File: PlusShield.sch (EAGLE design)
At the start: 32 parts, among them K1 G6J-2P-Y, K2 G6J-2P-Y

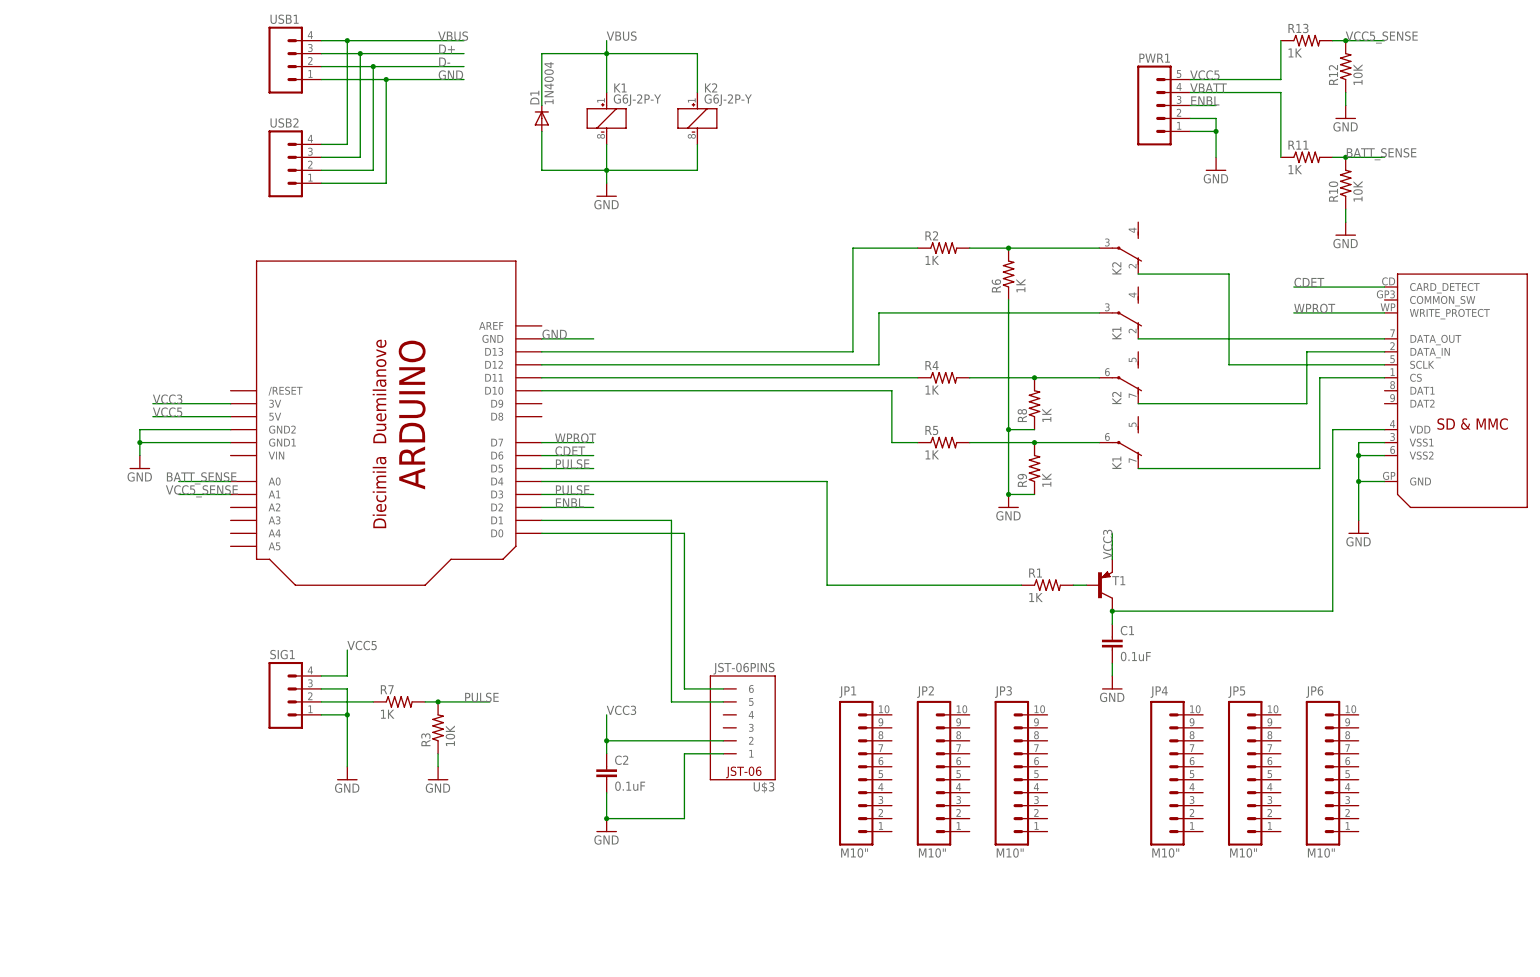
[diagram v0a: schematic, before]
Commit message: Added bigger proto area. Extra holes for arduino pins.
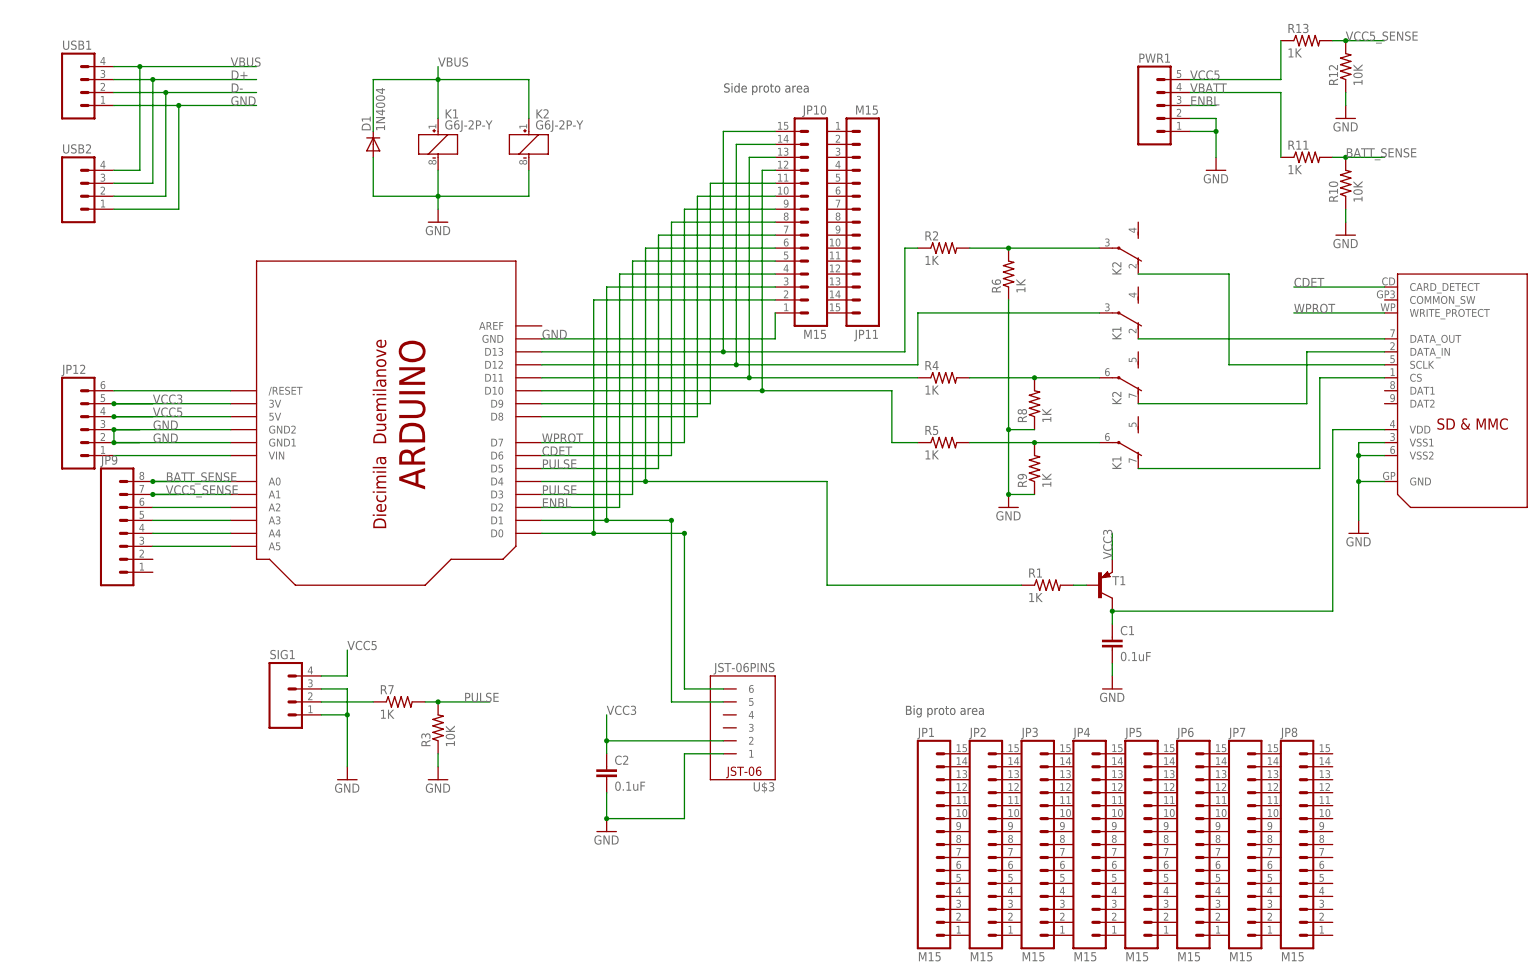
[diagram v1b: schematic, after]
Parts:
- added JP10, JP11, JP7, JP8: M15, SparkFun:M15
- added JP12: (no value), SparkFun:M06SIP
- added JP9: (no value), SparkFun:M08
- JP1, JP2, JP3, JP4, JP5, JP6: value M10" -> M15; device SparkFun:M10" -> SparkFun:M15
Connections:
- new net N$18: JP10.10, U$2.D8
- new net N$19: JP12.1, U$2.VIN
- new net N$20: JP12.6, U$2./RESET
- new net N$21: JP9.3, U$2.A5
- new net N$22: JP9.4, U$2.A4
- new net N$23: JP9.5, U$2.A3
- new net N$24: JP9.6, U$2.A2
- new net N$4: JP10.11, U$2.D9
- net BATT_SENSE: now also JP9.8
- net CDET: now also JP10.8
- net ENBL: now also JP10.4
- net GND: now also JP10.1, JP12.2, JP12.3
- net N$1: now also JP10.6
- net N$12: now also JP10.14
- net N$15: now also JP10.2
- net N$16: now also JP10.3
- net N$3: now also JP10.15
- net N$5: now also JP10.13
- net N$6: now also JP10.12
- net PULSE: now also JP10.5, JP10.7
- net VCC3: now also JP12.5
- net VCC5: now also JP12.4
- net VCC5_SENSE: now also JP9.7
- net WPROT: now also JP10.9
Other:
- note added: "Big proto area"
- note added: "Side proto area"
- moved on the sheet: D1, K1, K2, USB1, USB2

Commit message: Moved USB connector to other side. Added some labels on silkscreen. Put strain relief holes for Inspector connection. Moved board boundary. Added breakout USB connector dongle.
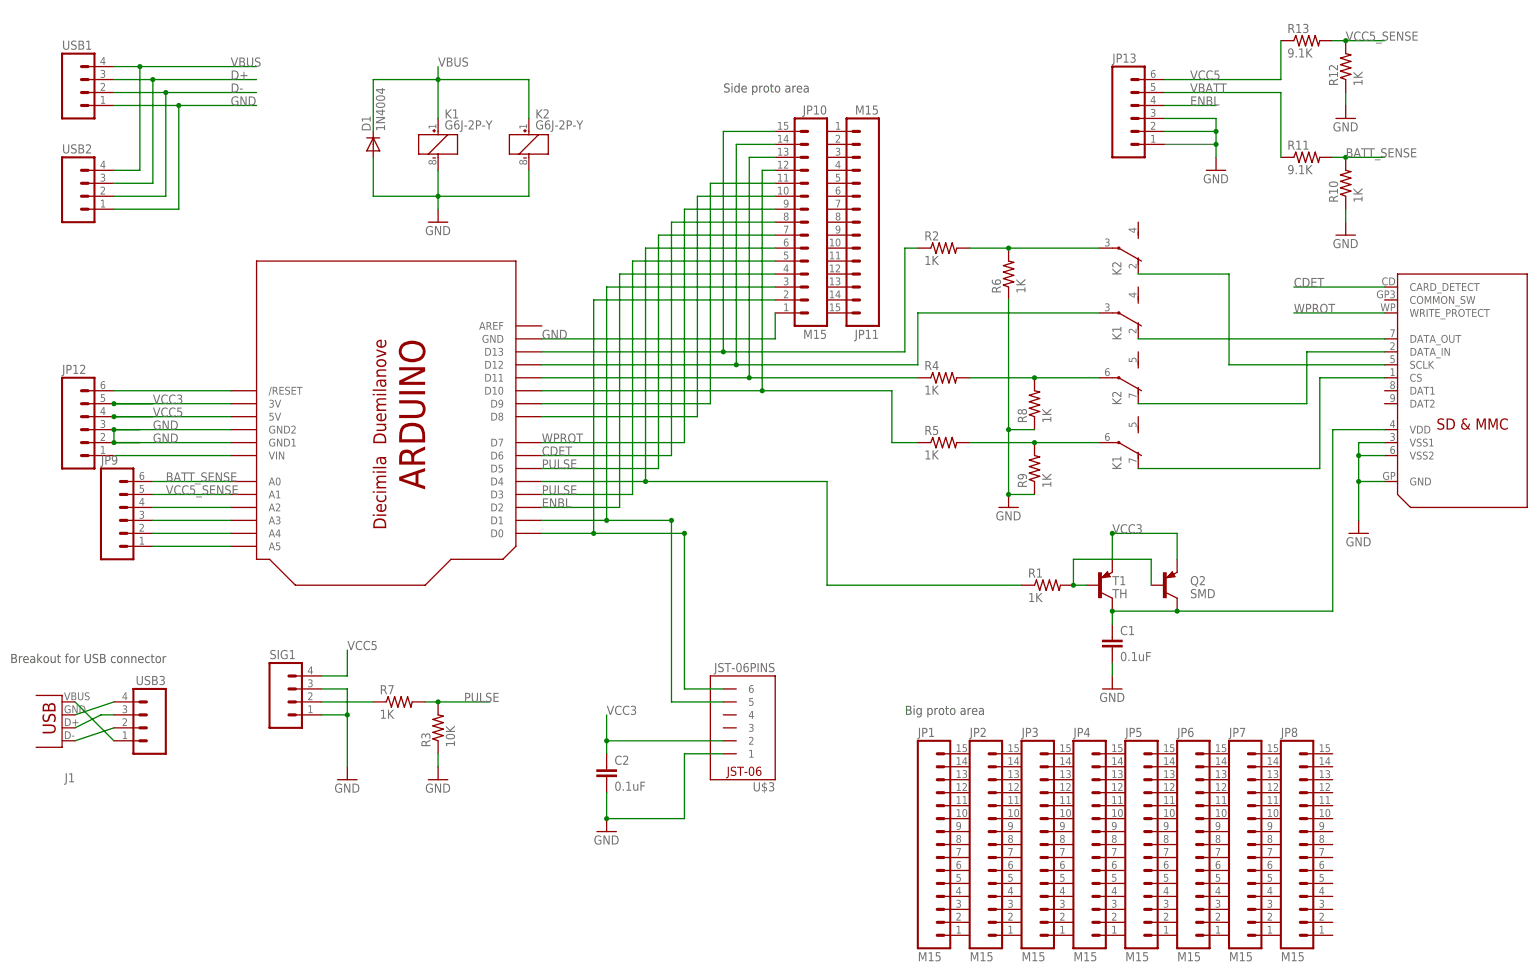
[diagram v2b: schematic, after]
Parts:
- removed PWR1: (no value), SparkFun:M05PTH
- added J1: (no value), SeeedConnector:USB-A-DIP
- added JP13: (no value), SparkFun:M06SIP
- added Q2: SMD, transistor-pnp:MMBTA56-SOT23
- added USB3: (no value), SparkFun:M04PTH
- JP9: device SparkFun:M08 -> SparkFun:M06SIP
- R10, R12: value 10K -> 1K
- R11, R13: value 1K -> 9.1K
- T1: value (none) -> TH; device transistor:-PNP-TO5 -> transistor-pnp:MPSA56-TO92
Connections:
- new net D+_C: J1.D-, USB3.3
- new net D-_C: J1.D+, USB3.2
- new net GND_C: J1.VBUS, USB3.4
- new net VBUS_C: J1.GND, USB3.1
- net BATT_SENSE: now also JP9.6; no longer JP9.8
- net ENBL: now also JP13.4; no longer PWR1.3
- net GND: now also JP13.2, JP13.3; no longer PWR1.1, PWR1.2
- net N$2: now also Q2.B
- net N$21: now also JP9.1; no longer JP9.3
- net N$22: now also JP9.2; no longer JP9.4
- net N$23: now also JP9.3; no longer JP9.5
- net N$24: now also JP9.4; no longer JP9.6
- net VBATT: now also JP13.5; no longer PWR1.4
- net VCC3: now also Q2.E
- net VCC5: now also JP13.6; no longer PWR1.5
- net VCC5_SENSE: now also JP9.5; no longer JP9.7
- net VDD: now also Q2.C
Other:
- note added: "Breakout for USB connector"

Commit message: Added switch pins. Moved stuff around. Extra connector for GPS.
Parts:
- added C3: 100uF, SparkFun:CAP_POL7343
- added GPS2: (no value), SparkFun:M04PTH
- added SWI: (no value), SparkFun:M02PTH
- R2, R4, R5: value 1K -> 10K
- R6, R8, R9: value 1K -> 15K
- renumbered U$3 to GPS1
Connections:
- removed net N$15: GPS1.6, JP10.2, U$2.D0
- removed net N$16: GPS1.5, JP10.3, U$2.D1
- new net 5VIN: C3.+, JP13.6, SWI.1
- new net RX: GPS1.6, GPS2.4, JP10.2, U$2.D0
- new net TX: GPS1.5, GPS2.3, JP10.3, U$2.D1
- net GND: now also C3.-, GPS2.1, JP13.1; no longer JP13.3
- net VBUS: now also JP13.3
- net VCC3: now also GPS2.2
- net VCC5: now also SWI.2; no longer JP13.6
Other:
- note added: "PlusShield v1.0"
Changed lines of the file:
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@@
 <part name="K1" library="relay" deviceset="G6J*-2?-Y" device="P"/>
 <part name="K2" library="relay" deviceset="G6J*-2?-Y" device="P"/>
-<part name="R2" library="adafruit" deviceset="R-US_" device="0207/10" value="1K"/>
-<part name="R4" library="adafruit" deviceset="R-US_" device="0207/10" value="1K"/>
-<part name="R5" library="adafruit" deviceset="R-US_" device="0207/10" value="1K"/>
-<part name="R6" library="adafruit" deviceset="R-US_" device="0207/10" value="1K"/>
-<part name="R8" library="adafruit" deviceset="R-US_" device="0207/10" value="1K"/>
-<part name="R9" library="adafruit" deviceset="R-US_" device="0207/10" value="1K"/>
+<part name="R2" library="adafruit" deviceset="R-US_" device="0207/10" value="10K"/>
+<part name="R4" library="adafruit" deviceset="R-US_" device="0207/10" value="10K"/>
+<part name="R5" library="adafruit" deviceset="R-US_" device="0207/10" value="10K"/>
+<part name="R6" library="adafruit" deviceset="R-US_" device="0207/10" value="15K"/>
+<part name="R8" library="adafruit" deviceset="R-US_" device="0207/10" value="15K"/>
+<part name="R9" library="adafruit" deviceset="R-US_" device="0207/10" value="15K"/>
 <part name="GND4" library="supply1" deviceset="GND" device=""/>
-<part name="U$3" library="Robin" deviceset="JST-06PINS" device=""/>
+<part name="GPS1" library="Robin" deviceset="JST-06PINS" device=""/>
 <part name="C2" library="SparkFun" deviceset="CAP" device="PTH1" value="0.1uF"/>
 <part name="GND5" library="supply1" deviceset="GND" device=""/>
@@
 <part name="USB3" library="SparkFun" deviceset="M04" device="PTH"/>
 <part name="Q2" library="transistor-pnp" deviceset="*-?" device="SOT23" technology="MMBTA56" value="SMD"/>
+<part name="GPS2" library="SparkFun" deviceset="M04" device="PTH"/>
+<part name="C3" library="SparkFun" deviceset="CAP_POL" device="7343" value="100uF"/>
+<part name="GND1" library="supply1" deviceset="GND" device=""/>
+<part name="SWI" library="SparkFun" deviceset="M02" device="PTH"/>
 </parts>
 <sheets>
@@
 <text x="58.42" y="104.14" size="1.778" layer="97">Side proto area</text>
 <text x="93.98" y="-17.78" size="1.778" layer="97">Big proto area</text>
-<wire x1="144.78" y1="93.98" x2="154.94" y2="93.98" width="0.1524" layer="97"/>
 <text x="-81.28" y="-7.62" size="1.778" layer="97">Breakout for USB connector</text>
+<text x="-73.66" y="-55.88" size="7.62" layer="97">PlusShield v1.0</text>
 </plain>
 <instances>
@@
 <instance part="R9" gate="G$1" x="119.38" y="30.48" rot="R90"/>
 <instance part="GND4" gate="1" x="114.3" y="22.86"/>
-<instance part="U$3" gate="G$1" x="58.42" y="-17.78" rot="R180"/>
+<instance part="GPS1" gate="G$1" x="58.42" y="-17.78" rot="R180"/>
 <instance part="C2" gate="G$1" x="35.56" y="-30.48"/>
 <instance part="GND5" gate="1" x="35.56" y="-40.64"/>
@@
 <attribute name="VALUE" x="149.86" y="5.08" size="1.778" layer="96"/>
 </instance>
+<instance part="GPS2" gate="G$1" x="78.74" y="-22.86" rot="MR0"/>
+<instance part="C3" gate="G$1" x="119.38" y="104.14"/>
+<instance part="GND1" gate="1" x="119.38" y="93.98"/>
+<instance part="SWI" gate="G$1" x="152.4" y="116.84" rot="R270"/>
 </instances>
 <busses>
@@
 </segment>
 <segment>
-<pinref part="U$3" gate="G$1" pin="2"/>
+<pinref part="GPS1" gate="G$1" pin="2"/>
 <wire x1="58.42" y1="-22.86" x2="35.56" y2="-22.86" width="0.1524" layer="91"/>
 <junction x="35.56" y="-22.86"/>
@@
 <wire x1="35.56" y1="-22.86" x2="35.56" y2="-17.78" width="0.1524" layer="91"/>
 <label x="35.56" y="-17.78" size="1.778" layer="95"/>
+<junction x="58.42" y="-22.86"/>
+<pinref part="GPS2" gate="G$1" pin="2"/>
+<wire x1="58.42" y1="-22.86" x2="73.66" y2="-22.86" width="0.1524" layer="91"/>
 </segment>
 </net>
@@
 </segment>
 <segment>
-<label x="149.86" y="106.68" size="1.778" layer="95"/>
+<label x="157.48" y="106.68" size="1.778" layer="95"/>
 <pinref part="R13" gate="G$1" pin="1"/>
-<wire x1="144.78" y1="106.68" x2="167.64" y2="106.68" width="0.1524" layer="91"/>
 <wire x1="167.64" y1="106.68" x2="167.64" y2="114.3" width="0.1524" layer="91"/>
-<pinref part="JP13" gate="G$1" pin="6"/>
+<pinref part="SWI" gate="G$1" pin="2"/>
+<wire x1="167.64" y1="106.68" x2="154.94" y2="106.68" width="0.1524" layer="91"/>
+<wire x1="154.94" y1="106.68" x2="154.94" y2="109.22" width="0.1524" layer="91"/>
 </segment>
 </net>
@@
 <wire x1="35.56" y1="-38.1" x2="50.8" y2="-38.1" width="0.1524" layer="91"/>
 <wire x1="50.8" y1="-38.1" x2="50.8" y2="-25.4" width="0.1524" layer="91"/>
-<pinref part="U$3" gate="G$1" pin="1"/>
+<pinref part="GPS1" gate="G$1" pin="1"/>
 <wire x1="50.8" y1="-25.4" x2="58.42" y2="-25.4" width="0.1524" layer="91"/>
 <junction x="35.56" y="-38.1"/>
+<junction x="58.42" y="-25.4"/>
+<pinref part="GPS2" gate="G$1" pin="1"/>
+<wire x1="58.42" y1="-25.4" x2="73.66" y2="-25.4" width="0.1524" layer="91"/>
 </segment>
 <segment>
@@
 <segment>
 <pinref part="GND9" gate="1" pin="GND"/>
-<wire x1="144.78" y1="99.06" x2="154.94" y2="99.06" width="0.1524" layer="91"/>
-<wire x1="154.94" y1="99.06" x2="154.94" y2="96.52" width="0.1524" layer="91"/>
-<junction x="154.94" y="96.52"/>
 <wire x1="154.94" y1="96.52" x2="154.94" y2="93.98" width="0.1524" layer="91"/>
 <wire x1="154.94" y1="93.98" x2="154.94" y2="91.44" width="0.1524" layer="91"/>
 <wire x1="144.78" y1="96.52" x2="154.94" y2="96.52" width="0.1524" layer="91"/>
 <pinref part="JP13" gate="G$1" pin="2"/>
-<pinref part="JP13" gate="G$1" pin="3"/>
 <junction x="154.94" y="93.98"/>
+<pinref part="JP13" gate="G$1" pin="1"/>
+<wire x1="154.94" y1="93.98" x2="144.78" y2="93.98" width="0.1524" layer="91"/>
 </segment>
 <segment>
@@
 <label x="-53.34" y="35.56" size="1.778" layer="95"/>
 </segment>
+<segment>
+<pinref part="C3" gate="G$1" pin="-"/>
+<pinref part="GND1" gate="1" pin="GND"/>
+<wire x1="119.38" y1="99.06" x2="119.38" y2="96.52" width="0.1524" layer="91"/>
+</segment>
 </net>
 <net name="N$7" class="0">
@@
 </segment>
 </net>
-<net name="N$15" class="0">
-<segment>
-<pinref part="U$3" gate="G$1" pin="6"/>
+<net name="RX" class="0">
+<segment>
+<pinref part="GPS1" gate="G$1" pin="6"/>
 <wire x1="58.42" y1="-12.7" x2="50.8" y2="-12.7" width="0.1524" layer="91"/>
 <wire x1="50.8" y1="-12.7" x2="50.8" y2="17.78" width="0.1524" layer="91"/>
 <pinref part="U$2" gate="G$1" pin="D0"/>
 <wire x1="50.8" y1="17.78" x2="33.02" y2="17.78" width="0.1524" layer="91"/>
-<junction x="50.8" y="17.78"/>
 <junction x="33.02" y="17.78"/>
 <wire x1="33.02" y1="17.78" x2="22.86" y2="17.78" width="0.1524" layer="91"/>
@@
 <wire x1="33.02" y1="17.78" x2="33.02" y2="63.5" width="0.1524" layer="91"/>
 <wire x1="33.02" y1="63.5" x2="68.58" y2="63.5" width="0.1524" layer="91"/>
-</segment>
-</net>
-<net name="N$16" class="0">
-<segment>
-<pinref part="U$3" gate="G$1" pin="5"/>
+<junction x="58.42" y="-12.7"/>
+<pinref part="GPS2" gate="G$1" pin="4"/>
+<wire x1="58.42" y1="-12.7" x2="73.66" y2="-12.7" width="0.1524" layer="91"/>
+<wire x1="73.66" y1="-12.7" x2="73.66" y2="-17.78" width="0.1524" layer="91"/>
+</segment>
+</net>
+<net name="TX" class="0">
+<segment>
+<pinref part="GPS1" gate="G$1" pin="5"/>
 <wire x1="58.42" y1="-15.24" x2="48.26" y2="-15.24" width="0.1524" layer="91"/>
 <wire x1="48.26" y1="-15.24" x2="48.26" y2="20.32" width="0.1524" layer="91"/>
 <pinref part="U$2" gate="G$1" pin="D1"/>
 <wire x1="48.26" y1="20.32" x2="35.56" y2="20.32" width="0.1524" layer="91"/>
-<junction x="48.26" y="20.32"/>
 <junction x="35.56" y="20.32"/>
 <wire x1="35.56" y1="20.32" x2="22.86" y2="20.32" width="0.1524" layer="91"/>
@@
 <wire x1="35.56" y1="20.32" x2="35.56" y2="66.04" width="0.1524" layer="91"/>
 <wire x1="35.56" y1="66.04" x2="68.58" y2="66.04" width="0.1524" layer="91"/>
+<junction x="58.42" y="-15.24"/>
+<wire x1="58.42" y1="-15.24" x2="71.12" y2="-15.24" width="0.1524" layer="91"/>
+<wire x1="71.12" y1="-15.24" x2="71.12" y2="-20.32" width="0.1524" layer="91"/>
+<pinref part="GPS2" gate="G$1" pin="3"/>
+<wire x1="71.12" y1="-20.32" x2="73.66" y2="-20.32" width="0.1524" layer="91"/>
 </segment>
 </net>
@@
 <label x="2.54" y="109.22" size="1.778" layer="95"/>
 </segment>
+<segment>
+<pinref part="JP13" gate="G$1" pin="3"/>
+<wire x1="144.78" y1="99.06" x2="154.94" y2="99.06" width="0.1524" layer="91"/>
+<label x="149.86" y="99.06" size="1.778" layer="95"/>
+</segment>
 </net>
 <net name="D+" class="0">
@@
 </segment>
 </net>
+<net name="5VIN" class="0">
+<segment>
+<pinref part="JP13" gate="G$1" pin="6"/>
+<pinref part="SWI" gate="G$1" pin="1"/>
+<wire x1="144.78" y1="106.68" x2="152.4" y2="106.68" width="0.1524" layer="91"/>
+<wire x1="152.4" y1="106.68" x2="152.4" y2="109.22" width="0.1524" layer="91"/>
+<label x="147.32" y="106.68" size="1.778" layer="95"/>
+</segment>
+<segment>
+<pinref part="C3" gate="G$1" pin="+"/>
+<wire x1="119.38" y1="106.68" x2="119.38" y2="111.76" width="0.1524" layer="91"/>
+<label x="119.38" y="111.76" size="1.778" layer="95"/>
+</segment>
+</net>
